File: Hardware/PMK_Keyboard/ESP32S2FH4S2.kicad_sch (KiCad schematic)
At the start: 27 parts, among them U401 ESP32-S2FH4, Y401 40MHz

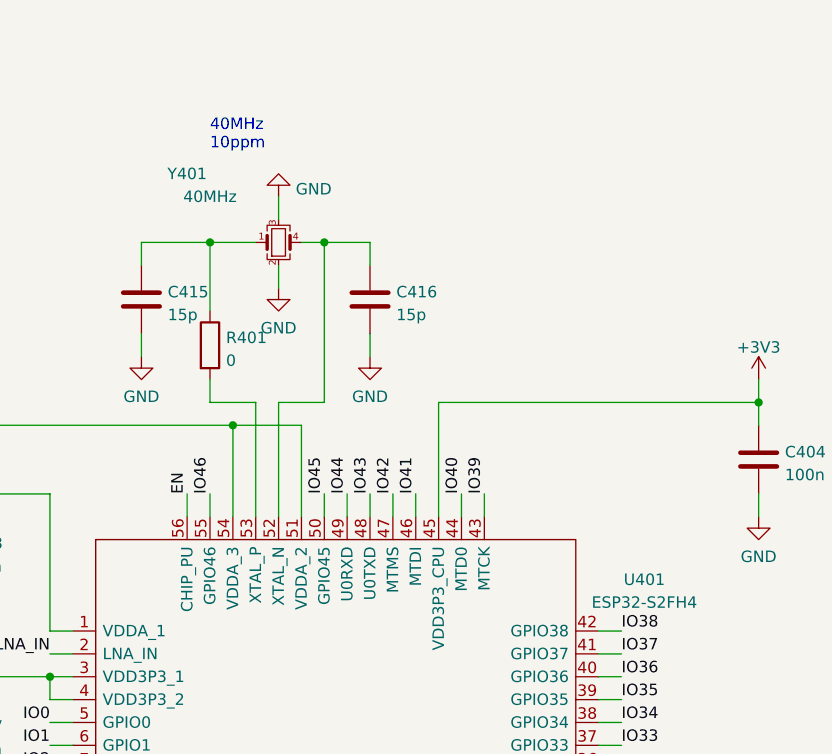
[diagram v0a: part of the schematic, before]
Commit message: Worked on hierachic page again
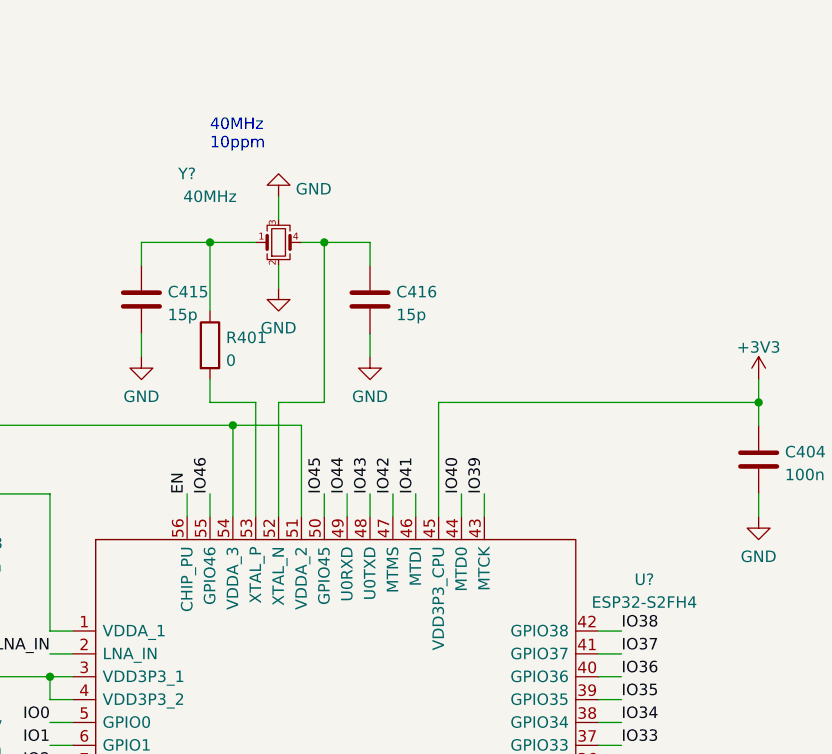
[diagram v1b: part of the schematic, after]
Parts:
- renumbered U401 to U?, Y401 to Y?
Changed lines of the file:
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@@
   (symbol (lib_id "Device:Crystal_GND23_Small") (at 91.44 63.5 0) (unit 1)
     (in_bom yes) (on_board yes)
-    (property "Reference" "Y401" (id 0) (at 81.28 55.88 0))
+    (property "Reference" "Y?" (id 0) (at 81.28 55.88 0))
     (property "Value" "40MHz" (id 1) (at 83.82 58.42 0))
     (property "Footprint" "Component_lib:Crystal_SMD_2016-4Pin_2.0x1.6mm" (id 2) (at 91.44 63.5 0)
@@
   (symbol (lib_id "Component_lib:ESP32-S2FH4") (at 68.58 106.68 0) (unit 1)
     (in_bom yes) (on_board yes) (fields_autoplaced)
-    (property "Reference" "U401" (id 0) (at 132.0844 100.9735 0))
+    (property "Reference" "U?" (id 0) (at 132.0844 100.9735 0))
     (property "Value" "ESP32-S2FH4" (id 1) (at 132.0844 103.5104 0))
     (property "Footprint" "QFN40P700X700X90-57N-D" (id 2) (at 134.62 111.76 0)

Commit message: Worked on hierachic sheet
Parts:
- gave numbers to parts that had none: 2
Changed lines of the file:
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@@
+    (stroke (width 0) (type default) (color 0 0 0 0))
+  )
+  (wire (pts (xy 270.51 25.4) (xy 271.78 25.4))
     (stroke (width 0) (type default) (color 0 0 0 0))
   )
@@
     (stroke (width 0) (type default) (color 0 0 0 0))
   )
+  (wire (pts (xy 271.78 58.42) (xy 270.51 58.42))
+    (stroke (width 0) (type default) (color 0 0 0 0))
+  )
   (wire (pts (xy 127 111.76) (xy 129.54 111.76))
     (stroke (width 0) (type default) (color 0 0 0 0))
@@
     (stroke (width 0) (type default) (color 0 0 0 0))
   )
+  (wire (pts (xy 270.51 24.13) (xy 270.51 25.4))
+    (stroke (width 0) (type default) (color 0 0 0 0))
+  )
   (wire (pts (xy 73.66 165.1) (xy 93.98 165.1))
     (stroke (width 0) (type default) (color 0 0 0 0))
@@
     (stroke (width 0) (type default) (color 0 0 0 0))
   )
+  (wire (pts (xy 270.51 34.29) (xy 271.78 34.29))
+    (stroke (width 0) (type default) (color 0 0 0 0))
+  )
   (wire (pts (xy 187.96 137.16) (xy 187.96 139.7))
     (stroke (width 0) (type default) (color 0 0 0 0))
@@
     (stroke (width 0) (type default) (color 0 0 0 0))
   )
+  (wire (pts (xy 270.51 58.42) (xy 270.51 59.69))
+    (stroke (width 0) (type default) (color 0 0 0 0))
+  )
   (wire (pts (xy 101.6 152.4) (xy 101.6 154.94))
     (stroke (width 0) (type default) (color 0 0 0 0))
@@
   )
   (wire (pts (xy 33.02 109.22) (xy 33.02 111.76))
+    (stroke (width 0) (type default) (color 0 0 0 0))
+  )
+  (wire (pts (xy 270.51 30.48) (xy 271.78 30.48))
     (stroke (width 0) (type default) (color 0 0 0 0))
   )
@@
     (effects (font (size 1.27 1.27)) (justify left bottom))
   )
+  (label "D-" (at 270.51 34.29 180)
+    (effects (font (size 1.27 1.27)) (justify right bottom))
+  )
+  (label "D+" (at 270.51 30.48 180)
+    (effects (font (size 1.27 1.27)) (justify right bottom))
+  )
+  (hierarchical_label "SR_CS" (shape bidirectional) (at 271.78 49.53 0)
+    (effects (font (size 1.27 1.27)) (justify left))
+  )
+  (hierarchical_label "LED_MOSI" (shape output) (at 271.78 38.1 0)
+    (effects (font (size 1.27 1.27)) (justify left))
+  )
+  (hierarchical_label "SR_CLK" (shape bidirectional) (at 271.78 45.72 0)
+    (effects (font (size 1.27 1.27)) (justify left))
+  )
+  (hierarchical_label "+3V3" (shape input) (at 271.78 25.4 0)
+    (effects (font (size 1.27 1.27)) (justify left))
+  )
+  (hierarchical_label "D+" (shape bidirectional) (at 271.78 30.48 0)
+    (effects (font (size 1.27 1.27)) (justify left))
+  )
+  (hierarchical_label "GND" (shape passive) (at 271.78 58.42 0)
+    (effects (font (size 1.27 1.27)) (justify left))
+  )
+  (hierarchical_label "D-" (shape bidirectional) (at 271.78 34.29 0)
+    (effects (font (size 1.27 1.27)) (justify left))
+  )
+  (hierarchical_label "SR_MISO" (shape input) (at 271.78 41.91 0)
+    (effects (font (size 1.27 1.27)) (justify left))
+  )
+  (symbol (lib_id "power:+3V3") (at 270.51 24.13 0) (unit 1)
+    (in_bom yes) (on_board yes) (fields_autoplaced)
+    (property "Reference" "#PWR?" (id 0) (at 270.51 27.94 0)
+      (effects (font (size 1.27 1.27)) hide)
+    )
+    (property "Value" "+3V3" (id 1) (at 270.51 20.5542 0))
+    (property "Footprint" "" (id 2) (at 270.51 24.13 0)
+      (effects (font (size 1.27 1.27)) hide)
+    )
+    (property "Datasheet" "" (id 3) (at 270.51 24.13 0)
+      (effects (font (size 1.27 1.27)) hide)
+    )
+    (pin "1")
+  )
   (symbol (lib_id "power:GND") (at 91.44 58.42 180) (unit 1)
     (in_bom yes) (on_board yes) (fields_autoplaced)
@@
   )
   (symbol (lib_id "Component lib:2450AT18A100E") (at 190.5 93.98 0) (unit 1)
-    (in_bom yes) (on_board yes) (fields_autoplaced)
-    (property "Reference" "ANT?" (id 0) (at 192.532 88.7003 0)
-      (effects (font (size 1.27 1.27)) (justify left))
-    )
-    (property "Value" "2450AT18A100E" (id 1) (at 192.532 91.2372 0)
+    (in_bom yes) (on_board yes)
+    (property "Reference" "ANT401" (id 0) (at 193.04 86.36 0)
+      (effects (font (size 1.27 1.27)) (justify left))
+    )
+    (property "Value" "2450AT18A100E" (id 1) (at 193.04 88.9 0)
       (effects (font (size 1.27 1.27)) (justify left))
     )
@@
     (pin "1")
     (pin "2")
+  )
+  (symbol (lib_id "power:GND") (at 270.51 59.69 0) (unit 1)
+    (in_bom yes) (on_board yes) (fields_autoplaced)
+    (property "Reference" "#PWR?" (id 0) (at 270.51 66.04 0)
+      (effects (font (size 1.27 1.27)) hide)
+    )
+    (property "Value" "GND" (id 1) (at 270.51 64.1334 0))
+    (property "Footprint" "" (id 2) (at 270.51 59.69 0)
+      (effects (font (size 1.27 1.27)) hide)
+    )
+    (property "Datasheet" "" (id 3) (at 270.51 59.69 0)
+      (effects (font (size 1.27 1.27)) hide)
+    )
+    (pin "1")
   )
   (symbol (lib_id "Component lib:C") (at 144.78 139.7 0) (unit 1)
@@
   (symbol (lib_id "Component_lib:ESP32-S2FH4") (at 68.58 106.68 0) (unit 1)
     (in_bom yes) (on_board yes) (fields_autoplaced)
-    (property "Reference" "U?" (id 0) (at 132.0844 100.9735 0))
+    (property "Reference" "U401" (id 0) (at 132.0844 100.9735 0))
     (property "Value" "ESP32-S2FH4" (id 1) (at 132.0844 103.5104 0))
     (property "Footprint" "QFN40P700X700X90-57N-D" (id 2) (at 134.62 111.76 0)

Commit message: Again on hierachic sheet
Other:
- company: (none) -> PumaCorp
- title: (none) -> PMK_Keyboard
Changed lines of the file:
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@@
 (kicad_sch (version 20211123) (generator eeschema)
   (paper "A4")
+  (title_block
+    (title "PMK_Keyboard")
+    (date "2023-02-06")
+    (rev "HW00")
+    (company "PumaCorp")
+    (comment 1 "Design by: NdG")
+  )
   (junction (at 43.18 83.82) (diameter 0) (color 0 0 0 0)
   )
@@
     (stroke (width 0) (type default) (color 0 0 0 0))
   )
-  (wire (pts (xy 271.78 58.42) (xy 270.51 58.42))
+  (wire (pts (xy 271.78 62.23) (xy 270.51 62.23))
     (stroke (width 0) (type default) (color 0 0 0 0))
   )
@@
     (stroke (width 0) (type default) (color 0 0 0 0))
   )
-  (wire (pts (xy 270.51 58.42) (xy 270.51 59.69))
+  (wire (pts (xy 270.51 62.23) (xy 270.51 63.5))
     (stroke (width 0) (type default) (color 0 0 0 0))
   )
@@
     (effects (font (size 1.27 1.27)) (justify left))
   )
-  (hierarchical_label "GND" (shape passive) (at 271.78 58.42 0)
+  (hierarchical_label "GND" (shape passive) (at 271.78 62.23 0)
+    (effects (font (size 1.27 1.27)) (justify left))
+  )
+  (hierarchical_label "PL" (shape output) (at 271.78 53.34 0)
+    (effects (font (size 1.27 1.27)) (justify left))
+  )
+  (hierarchical_label "LED_EN" (shape output) (at 271.78 57.15 0)
     (effects (font (size 1.27 1.27)) (justify left))
   )
@@
     (pin "2")
   )
-  (symbol (lib_id "power:GND") (at 270.51 59.69 0) (unit 1)
-    (in_bom yes) (on_board yes) (fields_autoplaced)
-    (property "Reference" "#PWR?" (id 0) (at 270.51 66.04 0)
-      (effects (font (size 1.27 1.27)) hide)
-    )
-    (property "Value" "GND" (id 1) (at 270.51 64.1334 0))
-    (property "Footprint" "" (id 2) (at 270.51 59.69 0)
-      (effects (font (size 1.27 1.27)) hide)
-    )
-    (property "Datasheet" "" (id 3) (at 270.51 59.69 0)
-      (effects (font (size 1.27 1.27)) hide)
-    )
+  (symbol (lib_id "power:GND") (at 270.51 63.5 0) (unit 1)
+    (in_bom yes) (on_board yes) (fields_autoplaced)
+    (property "Reference" "#PWR?" (id 0) (at 270.51 69.85 0)
+      (effects (font (size 1.27 1.27)) hide)
+    )
+    (property "Value" "GND" (id 1) (at 270.51 67.9434 0))
+    (property "Footprint" "" (id 2) (at 270.51 63.5 0)
+      (effects (font (size 1.27 1.27)) hide)
+    )
+    (property "Datasheet" "" (id 3) (at 270.51 63.5 0)
+      (effects (font (size 1.27 1.27)) hide)
+    )

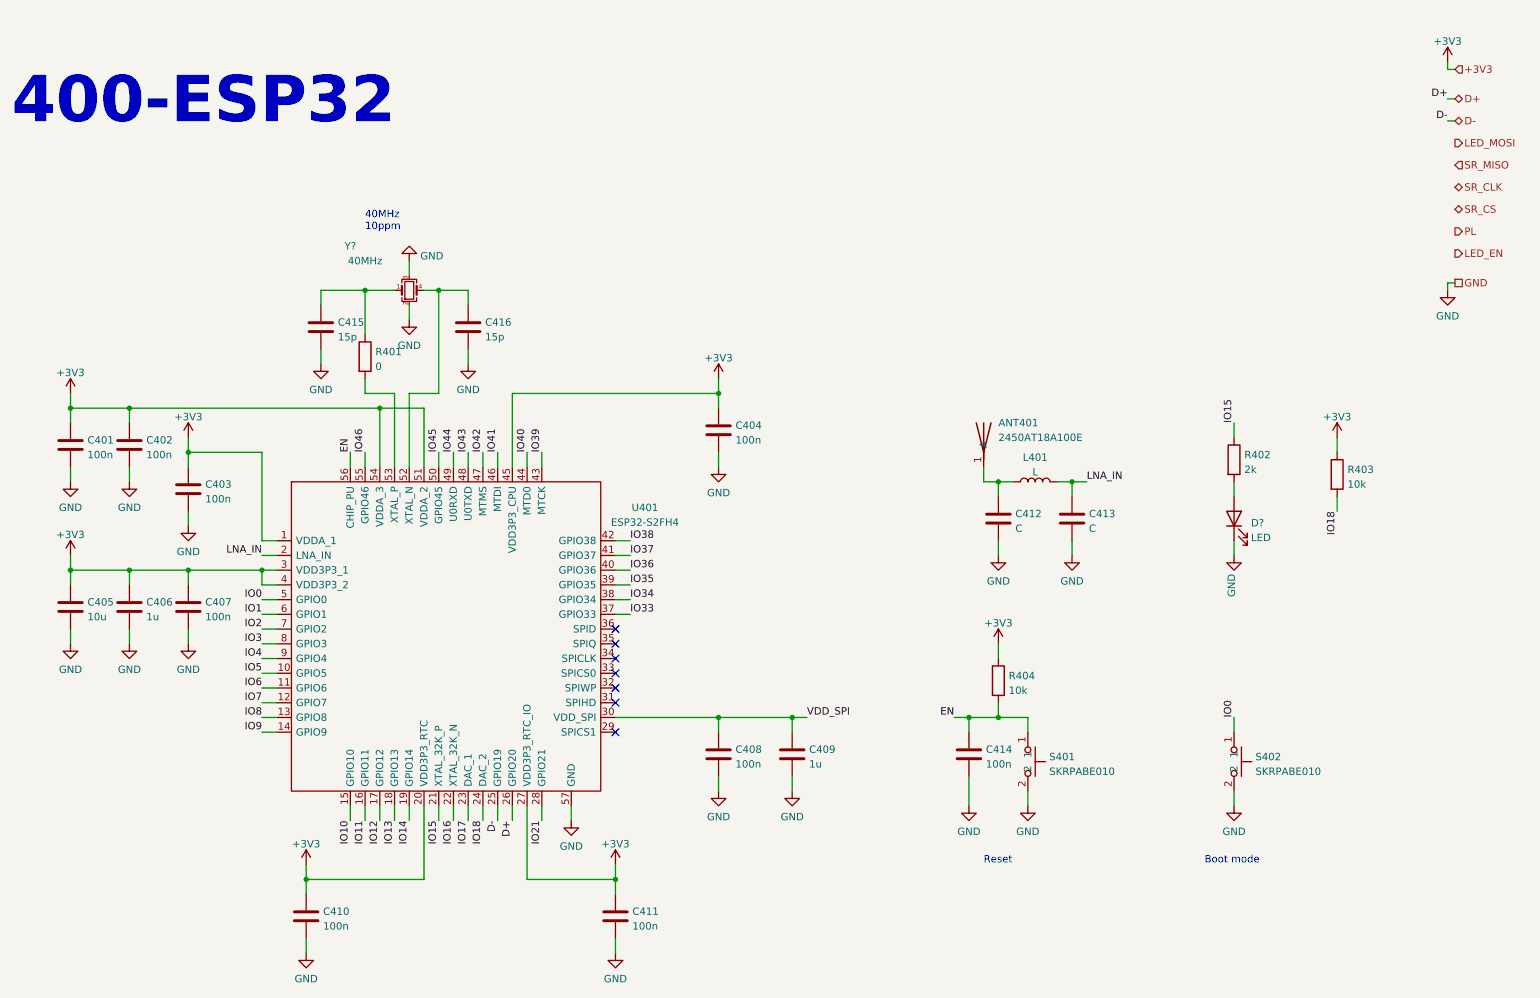
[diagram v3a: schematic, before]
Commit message: Schematic is done, only possible update is change of ESP pins
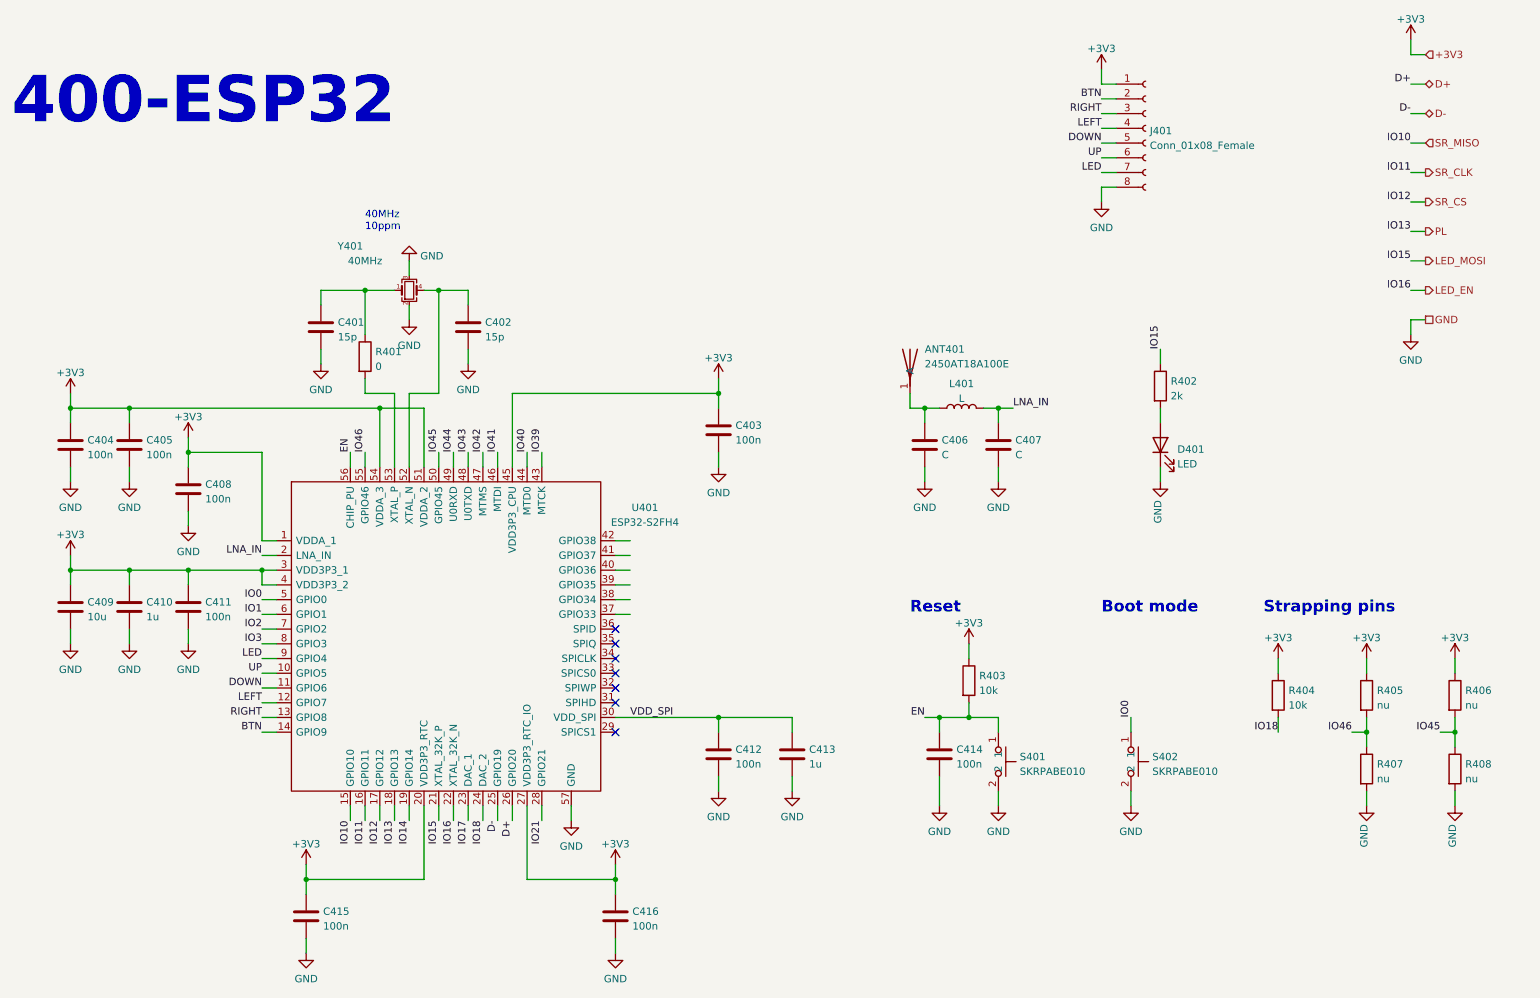
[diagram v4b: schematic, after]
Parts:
- added J401: Conn_01x08_Female, symbol Connector:Conn_01x08_Female
- added R405, R406, R407, R408: nu, Resistor_SMD:R_0201_0603Metric, symbol Component lib:R
- gave numbers to parts that had none: 2
- renumbered C415 to C401, C416 to C402, C404 to C403, C401 to C404, C402 to C405, C412 to C406, C413 to C407, C403 to C408, C405 to C409, C406 to C410, C407 to C411, C408 to C412, C409 to C413, C410 to C415, C411 to C416, R404 to R403, R403 to R404
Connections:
- net IO10 is gone; now on net SR_MISO: U401.15 (GPIO10)
- net IO11 is gone; now on net SR_CLK: U401.16 (GPIO11)
- net IO12 is gone; now on net SR_CS: U401.17 (GPIO12)
- net IO13 is gone; now on net PL: U401.18 (GPIO13)
- net IO15 is gone; now on net LED_MOSI: R402.1, U401.21 (XTAL_32K_P)
- net IO16 is gone; now on net LED_EN: U401.22 (XTAL_32K_N)
- net +3V3: now also J401.1 (Pin_1), R405.1, R406.1
- net GND: now also J401.8 (Pin_8), R407.2, R408.2
- net IO45: now also R406.2, R408.1
- net IO46: now also R405.2, R407.1
- net IO33: no longer names the net of U401.37 (GPIO33)
- net IO34: no longer names the net of U401.38 (GPIO34)
- net IO35: no longer names the net of U401.39 (GPIO35)
- net IO36: no longer names the net of U401.40 (GPIO36)
- net IO37: no longer names the net of U401.41 (GPIO37)
- net IO38: no longer names the net of U401.42 (GPIO38)
- net IO4 renamed LED
- net LED: now also J401.7 (Pin_7)
- net IO5 renamed UP
- net UP: now also J401.6 (Pin_6)
- net IO6 renamed DOWN
- net DOWN: now also J401.5 (Pin_5)
- net IO7 renamed LEFT
- net LEFT: now also J401.4 (Pin_4)
- net IO8 renamed RIGHT
- net RIGHT: now also J401.3 (Pin_3)
- net IO9 renamed BTN
- net BTN: now also J401.2 (Pin_2)
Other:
- note added: "Strapping pins"
- moved on the sheet: ANT401, C406, C407, C414, D401, L401, R402, R403, R404, S401, S402

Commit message: Routing is finally updated
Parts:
- J401: footprint (none) -> Connector_PinHeader_1.00mm:PinHeader_1x08_P1.00mm_Vertical
- U401: footprint QFN40P700X700X90-57N-D -> Component_lib:QFN40P700X700X90-57N-D
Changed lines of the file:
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@@
       (effects (font (size 1.27 1.27)) (justify left))
     )
-    (property "Footprint" "" (id 2) (at 218.44 35.56 0)
+    (property "Footprint" "Connector_PinHeader_1.00mm:PinHeader_1x08_P1.00mm_Vertical" (id 2) (at 218.44 35.56 0)
       (effects (font (size 1.27 1.27)) hide)
     )
@@
   (symbol (lib_id "power:GND") (at 210.82 48.26 0) (unit 1)
     (in_bom yes) (on_board yes) (fields_autoplaced)
-    (property "Reference" "#PWR?" (id 0) (at 210.82 54.61 0)
+    (property "Reference" "#PWR0119" (id 0) (at 210.82 54.61 0)
       (effects (font (size 1.27 1.27)) hide)
     )
@@
   (symbol (lib_id "power:+3V3") (at 210.82 25.4 0) (unit 1)
     (in_bom yes) (on_board yes) (fields_autoplaced)
-    (property "Reference" "#PWR?" (id 0) (at 210.82 29.21 0)
+    (property "Reference" "#PWR0120" (id 0) (at 210.82 29.21 0)
       (effects (font (size 1.27 1.27)) hide)
     )
@@
     (property "Reference" "U401" (id 0) (at 132.0844 100.9735 0))
     (property "Value" "ESP32-S2FH4" (id 1) (at 132.0844 103.5104 0))
-    (property "Footprint" "QFN40P700X700X90-57N-D" (id 2) (at 134.62 111.76 0)
-      (effects (font (size 1.27 1.27)) (justify left) hide)
-    )
+    (property "Footprint" "Component_lib:QFN40P700X700X90-57N-D" (id 2) (at 134.62 111.76 0)
+      (effects (font (size 1.27 1.27)) (justify left) hide)
+    )
